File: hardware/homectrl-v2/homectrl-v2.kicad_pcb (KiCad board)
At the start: 2 copper layers, 64 x 64 mm, 136 parts, among them J1 Barrel_Jack, J2 PUMP1_CONN, J3 PUMP2_CONN, J4 STEP_CONN, J5 USB_C_CONN, J6 SMS1_CONN, J7 ALS_CONN, J8 FSW1_CONN, Q1 AO3407A, Q2 2N7002, Q3 ZXMN3A01ZTA, Q4 ZXMN3A01ZTA, Q5 AO3400A, SW1 S3_RESET_SW, SW2 S3_BOOT_SW, U1 TPS5405DR, U2 MCP1826S, U3 DMP4065S-7, U4 ESP32-S3-WROOM-1, U5 TMC2209, U7 TPD4E001DRLR, U8 TPD2E001DRLR, U9 SI2347DS-T1-GE3

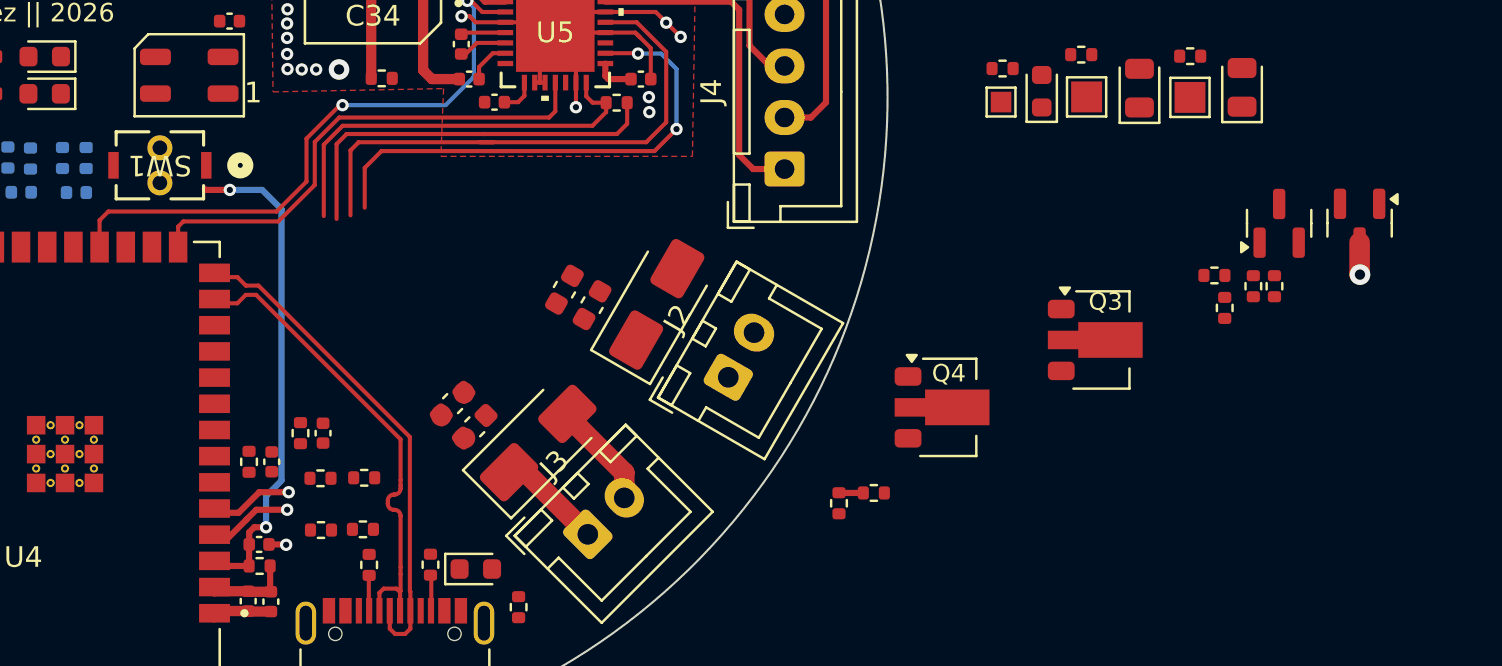
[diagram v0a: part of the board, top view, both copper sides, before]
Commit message: start signal routes
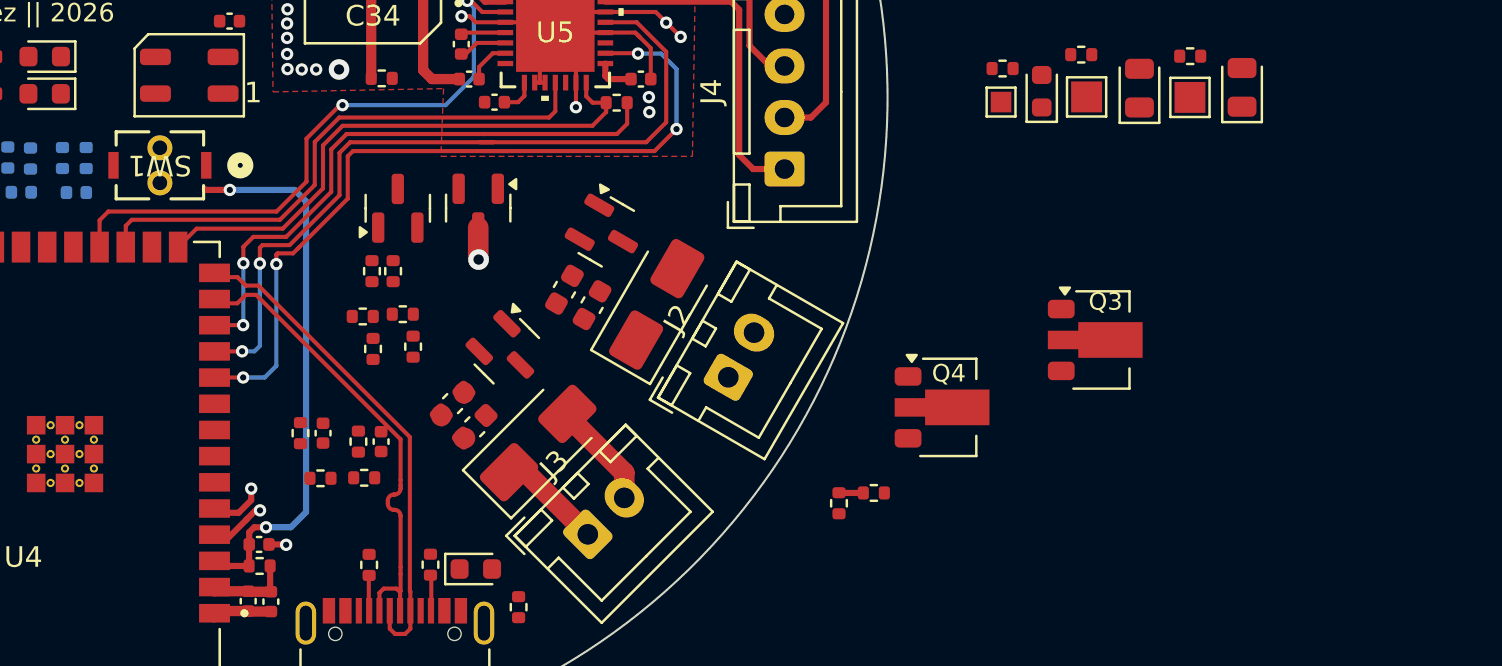
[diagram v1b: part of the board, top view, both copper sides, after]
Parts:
- removed R37: 13k, Resistor_SMD:R_0402_1005Metric
- removed R38: 20K, Resistor_SMD:R_0402_1005Metric
- added R22: 200, Resistor_SMD:R_0402_1005Metric, F.Cu at (134.0, 77.3)
- added R23: 10k, Resistor_SMD:R_0402_1005Metric, F.Cu at (134.5, 78.9)
- added REF**: SOT-23, Package_TO_SOT_SMD:SOT-23, F.Cu at (139.0, 79.1)
- added REF**: SOT-23, Package_TO_SOT_SMD:SOT-23, F.Cu at (143.8, 73.3)
- moved Q2 42.8 mm to (133.7, 72.2)
- moved R6 42.8 mm to (133.5, 75.2)
- moved R7 42.8 mm to (132.5, 75.2)
- moved U3 42.8 mm to (137.6, 72.1)
- moved R22 41.4 mm to (132.0, 77.4)
- moved R23 41.4 mm to (132.5, 79.0)
- moved C28 5.39 mm to (132.9, 83.5)
- moved R39 5.39 mm to (131.8, 83.5)
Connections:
- R22 pad 1: PUMP1_GATE -> PUMP1_EN
- R24 pad 1: PUMP2_GATE -> PUMP2_EN
- U4 pad 10: unconnected-(U4-IO17-Pad10) -> MTR_STEP
- U4 pad 11: unconnected-(U4-IO18-Pad11) -> MTR_DIR
- U4 pad 12: SMS1_DATA -> S3_RXD
- U4 pad 15: STEP_DIAG -> S3_TXD
- U4 pad 17: SMS2_DATA -> STEP_DIAG
- U4 pad 4: VCC_SENSE -> VPLUG_SENSE
- U4 pad 5: VPLUG_SENSE -> SMS1_DATA
- U4 pad 6: unconnected-(U4-IO6-Pad6) -> SMS2_DATA
- U4 pad 7: unconnected-(U4-IO7-Pad7) -> PUMP2_EN
- U4 pad 8: unconnected-(U4-IO15-Pad8) -> PUMP1_EN
- U4 pad 9: unconnected-(U4-IO16-Pad9) -> VPMP_EN
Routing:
- net MTR_STEP: track 25.7 -> 39.7 mm, vias 2 -> 4
- net MTR_DIR: track 26.6 -> 38.1 mm, vias 0 -> 2
- net S3_RXD: track 19.3 -> 28.7 mm, vias 0 -> 2
- net S3_TXD: track 20.0 -> 26.9 mm
- net VCC_SENSE: track 4.13 -> 0.00 mm, vias 1 -> 0
- net SMS1_DATA: track 0.00 -> 2.61 mm, vias 0 -> 1
- net S3_EN: track 24.1 -> 26.7 mm
- net STEP_DIAG: track 24.2 -> 26.8 mm
- net VPLUG_SENSE: track 4.03 -> 2.80 mm

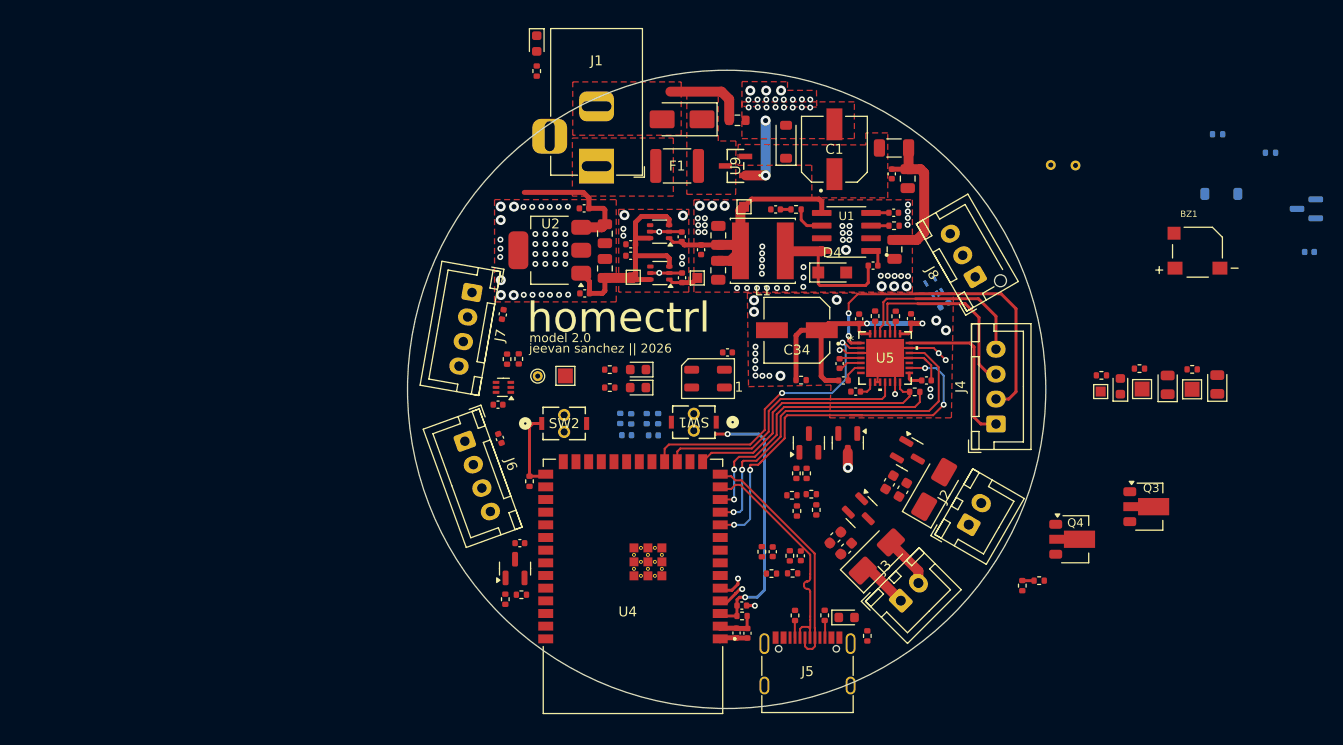
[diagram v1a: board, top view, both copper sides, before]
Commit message: more signal routing
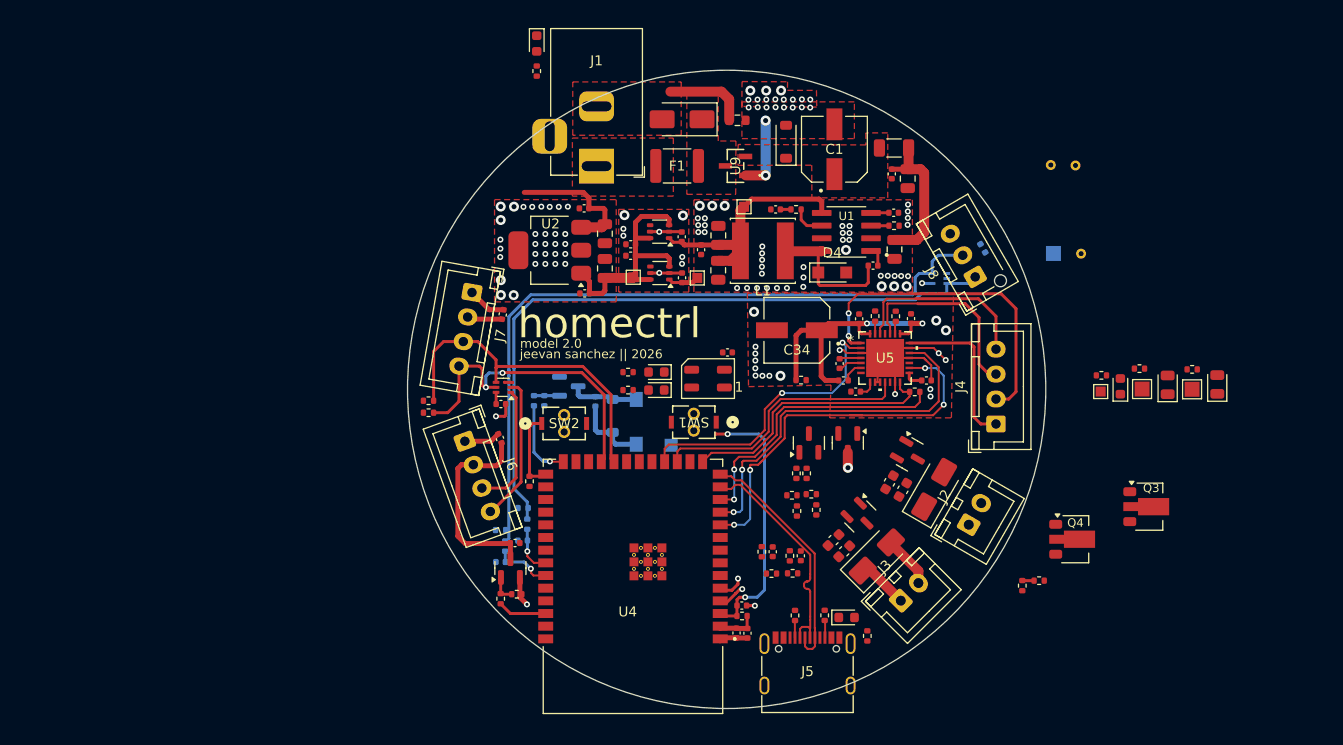
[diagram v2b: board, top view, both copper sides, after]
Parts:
- BZ1, TP1, TP3: moved to B.Cu
- moved R19 76.9 mm to (107.2, 67.9), turned to 90 degrees
- moved Q5 76.1 mm to (109.7, 66.5), turned to 0 degrees
- moved R16 73.6 mm to (106.2, 67.9), turned to -90 degrees
- moved C21 73.2 mm to (112.3, 68.0), turned to 90 degrees
- moved D13 65.0 mm to (114.1, 69.4), turned to 90 degrees
- moved BZ1 57.3 mm to (118.0, 70.0), turned to 90 degrees
- moved TP3 55.9 mm to (161.0, 53.2), turned to 180 degrees
- moved TP1 50.5 mm to (158.3, 53.1), turned to 180 degrees
- moved C24 17.9 mm to (102.8, 84.1), turned to 180 degrees
- moved R32 17.2 mm to (103.3, 82.5)
- moved R28 17.2 mm to (102.8, 80.9), turned to 0 degrees
- moved R27 16.9 mm to (105.5, 80.3)
- moved C32 16.8 mm to (105.0, 81.9), turned to 0 degrees
- moved R26 15.3 mm to (105.1, 78.7), turned to 0 degrees
- moved R34 10.5 mm to (95.6, 69.1), turned to 0 degrees
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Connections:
- C21 pad 2: GND -> Net-(D13-A)
- C24 pad 1: Net-(C24-Pad1) -> FSW2_SIG
- C32 pad 2: Net-(C32-Pad2) -> FSW1_SIG
- J6 pad 3: Net-(J6-Pin_3) -> SMS1_DATA
- J6 pad 4: Net-(J6-Pin_4) -> SMS2_DATA
- R27 pad 1: Net-(C32-Pad2) -> FSW1_SIG
- R32 pad 1: Net-(C24-Pad1) -> FSW2_SIG
- R39 pad 1: Net-(J6-Pin_3) -> SMS1_DATA
- R40 pad 1: Net-(J6-Pin_4) -> SMS2_DATA
- U4 pad 22: unconnected-(U4-IO14-Pad22) -> I2C_CLK
- U4 pad 23: unconnected-(U4-IO21-Pad23) -> I2C_DTA
- U4 pad 26: unconnected-(U4-IO45-Pad26) -> BUZZ_EN
- U4 pad 34: unconnected-(U4-IO41-Pad34) -> FSW1_SIG
- U4 pad 35: unconnected-(U4-IO42-Pad35) -> FSW2_SIG
- U4 pad 38: unconnected-(U4-IO2-Pad38) -> VPMP_EN
- U7 pad 1: SMS2_DATA -> SMS1_DATA
- U7 pad 2: SMS1_DATA -> SMS2_DATA
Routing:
- net FSW2_SIG: track 0.00 -> 78.1 mm, vias 0 -> 1
- net FSW1_SIG: track 0.83 -> 74.9 mm, vias 0 -> 1
- net I2C_CLK: track 0.00 -> 34.2 mm
- net I2C_DTA: track 0.00 -> 33.0 mm, vias 0 -> 2
- net VSMS: track 0.65 -> 21.2 mm
- net +3V3: track 19.3 -> 34.6 mm, vias 0 -> 1
- net SMS2_DATA: track 0.00 -> 14.6 mm
- net SMS1_DATA: track 2.61 -> 15.3 mm
- net GND: track 43.7 -> 55.0 mm, vias 128 -> 122
- net BUZZ_EN: track 0.00 -> 8.00 mm, vias 0 -> 1
- net Net-(D13-A): track 0.00 -> 6.88 mm
- net VPMP_EN: track 0.00 -> 4.92 mm
- net Net-(Q1-G): track 0.00 -> 2.73 mm
- net Net-(Q5-G): track 0.00 -> 2.57 mm

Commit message: finish component routing
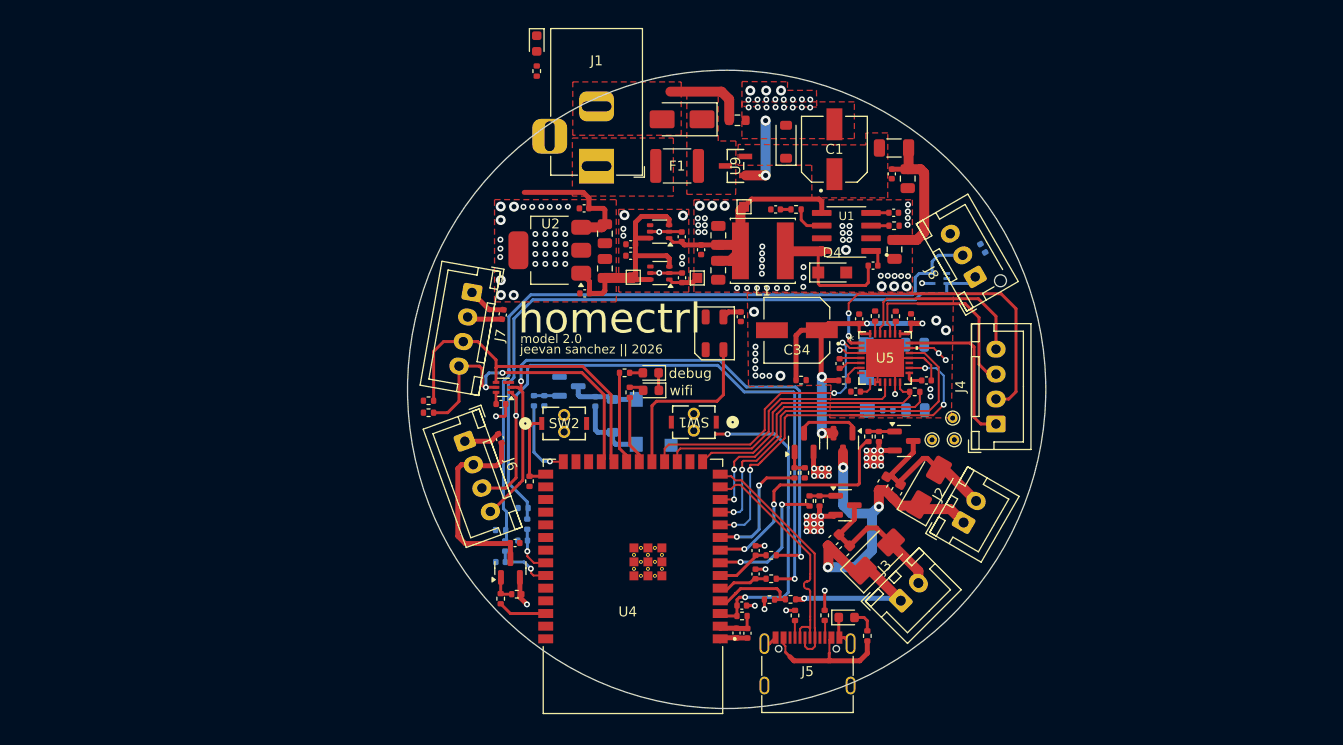
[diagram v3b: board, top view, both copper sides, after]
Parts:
- removed D10: PMP_V_LED, LED_SMD:LED_0603_1608Metric
- removed R15: 1k, Resistor_SMD:R_0402_1005Metric
- removed the R22 at (134.0, 77.3)
- removed the R23 at (134.5, 78.9)
- removed REF** (x2): SOT-23, Package_TO_SOT_SMD:SOT-23
- removed TP2: VMOT_TP_PAD, TestPoint:TestPoint_Pad_1.0x1.0mm
- D7, D8, R12, R13, TP5, TP9: moved to B.Cu
- Q3, Q4: value ZXMN3A01ZTA -> AO3400A; footprint Package_TO_SOT_SMD:SOT-89-3 -> Package_TO_SOT_SMD:SOT-23
- TP13, TP3, TP7: moved to F.Cu
- moved TP9 33.0 mm to (139.5, 62.3), turned to 180 degrees
- moved R13 30.7 mm to (141.6, 62.3)
- moved D8 30.6 mm to (144.4, 62.3), turned to 180 degrees
- moved TP7 30.1 mm to (148.3, 71.8), turned to -90 degrees
- moved TP13 30.0 mm to (146.1, 71.8), turned to -90 degrees
- moved TP5 27.6 mm to (139.6, 68.9), turned to 180 degrees
- moved R12 25.6 mm to (141.7, 68.9)
- moved Q3 25.5 mm to (143.3, 72.0)
- moved D7 25.4 mm to (144.4, 68.9), turned to 180 degrees
- moved R25 23.4 mm to (134.8, 78.0), turned to 90 degrees
- moved Q4 23.3 mm to (137.4, 78.4)
- moved R24 23.0 mm to (133.8, 78.0)
- moved TP1 22.5 mm to (139.5, 65.6)
- moved TP3 20.9 mm to (148.2, 69.7), turned to -90 degrees
- moved R23 11.1 mm to (140.8, 71.5)
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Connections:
- Q3 pad 2: PUMP1_N -> GND
- Q3 pad 3: GND -> PUMP1_N
- Q4 pad 2: PUMP2_N -> GND
- Q4 pad 3: GND -> PUMP2_N
- R8 pad 1: VPLUG -> VPMP
- U4 pad 19: unconnected-(U4-IO11-Pad19) -> RGB_DATA
- U4 pad 20: unconnected-(U4-IO12-Pad20) -> WIFI_LED
- U4 pad 21: unconnected-(U4-IO13-Pad21) -> DBG_LED
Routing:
- net SMS2_DATA: track 14.6 -> 71.4 mm, vias 0 -> 2
- net SMS1_DATA: track 15.3 -> 71.5 mm, vias 1 -> 2
- net GND: track 55.0 -> 106.3 mm, vias 122 -> 151
- net VPMP: track 7.12 -> 52.5 mm, vias 1 -> 4
- net PUMP1_EN: track 0.00 -> 23.2 mm, vias 0 -> 2
- net PUMP1_N: track 0.00 -> 17.8 mm
- net RGB_DATA: track 0.00 -> 17.8 mm
- net 5V_USB: track 3.12 -> 17.2 mm
- net PUMP2_EN: track 0.00 -> 14.0 mm, vias 0 -> 2
- net VPMP_EN: track 4.92 -> 17.4 mm, vias 0 -> 2
- net PUMP2_N: track 5.22 -> 15.8 mm
- net DBG_LED: track 0.00 -> 9.22 mm
- net WIFI_LED: track 0.00 -> 6.84 mm
- net VPLUG: track 44.2 -> 51.0 mm, vias 2 -> 4
- net Net-(Q2-D): track 0.00 -> 6.53 mm
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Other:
- board text added: "debug"
- board text added: "engineered by Jeevan Sanchez in Toronto, CA"
- board text added: "wifi"

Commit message: logic power routing
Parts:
- removed BZ1: SMT-0540-S-R, SMT-0540-S-R:XDCR_SMT-0540-S-R
- removed C21: 0.1uF, Capacitor_SMD:C_0402_1005Metric
- removed D13: 1N4148W, Diode_SMD:D_SOD-123
- removed Q5: AO3400A, Package_TO_SOT_SMD:SOT-23
- removed R16: 200, Resistor_SMD:R_0402_1005Metric
- removed R19: 10k, Resistor_SMD:R_0402_1005Metric
- added D8: 3V3_LED, LED_SMD:LED_0805_2012Metric, F.Cu at (107.8, 66.5)
- added R13: 200, Resistor_SMD:R_0402_1005Metric, F.Cu at (110.6, 66.5)
- D7: value BATT_LED -> PLUG_LED; footprint LED_SMD:LED_0805_2012Metric -> LED_SMD:LED_0603_1608Metric
- J8: footprint Connector_JST:JST_XH_B3B-XH-AM_1x03_P2.50mm_Vertical -> Connector_JST:JST_XH_B3B-XH-A_1x03_P2.50mm_Vertical
- R12: value 1k -> 1K
- TP1: moved to F.Cu
- moved TP13 24.2 mm to (169.2, 64.5)
- moved TP7 24.2 mm to (171.4, 64.5)
- moved TP3 20.2 mm to (128.0, 70.0)
- moved TP1 11.8 mm to (128.0, 67.8), turned to 0 degrees
- moved C31 5.11 mm to (147.0, 55.6), turned to 0 degrees
- moved U8 1.61 mm to (146.6, 57.2)
- moved J4 0.77 mm to (151.7, 70.2)
- moved J5 0.12 mm to (133.6, 95.5)
- turned R39 to 180 degrees
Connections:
- net VPLUG_SENSE renamed VPMP_SENSE
- J6 pad 3: SMS1_DATA -> Net-(J6-Pin_3)
- J6 pad 4: SMS2_DATA -> Net-(J6-Pin_4)
- J8 pad 1: FSW1_SIG -> Net-(J8-Pin_1)
- J8 pad 2: FSW2_SIG -> Net-(J8-Pin_2)
- R26 pad 2: FSW1_SIG -> Net-(J8-Pin_1)
- R27 pad 2: FSW1_SIG -> Net-(J8-Pin_1)
- R28 pad 2: FSW2_SIG -> Net-(J8-Pin_2)
- R32 pad 2: FSW2_SIG -> Net-(J8-Pin_2)
- R39 pad 1: SMS1_DATA -> Net-(J6-Pin_3)
- R40 pad 1: SMS2_DATA -> Net-(J6-Pin_4)
- U7 pad 1: SMS1_DATA -> Net-(J6-Pin_4)
- U7 pad 2: SMS2_DATA -> Net-(J6-Pin_3)
- U8 pad 3: FSW1_SIG -> Net-(J8-Pin_1)
- U8 pad 5: FSW2_SIG -> Net-(J8-Pin_2)
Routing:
- net +3V3: track 36.5 -> 199.6 mm, vias 1 -> 12
- net FSW2_SIG: track 78.4 -> 5.90 mm
- net FSW1_SIG: track 75.3 -> 4.83 mm
- net Net-(J8-Pin_2): track 0.00 -> 69.9 mm
- net Net-(J8-Pin_1): track 0.00 -> 68.8 mm
- net SMS1_DATA: track 71.5 -> 5.09 mm, vias 2 -> 0
- net Net-(J6-Pin_3): track 0.00 -> 66.4 mm, vias 0 -> 2
- net SMS2_DATA: track 71.4 -> 5.51 mm, vias 2 -> 0
- net Net-(J6-Pin_4): track 0.00 -> 65.7 mm, vias 0 -> 2
- net GND: track 106.3 -> 122.4 mm, vias 151 -> 152
- net BUZZ_EN: track 8.00 -> 0.00 mm, vias 1 -> 0
- net Net-(D13-A): track 6.88 -> 0.00 mm
- net VPLUG: track 51.0 -> 57.2 mm
- net Net-(D8-A): track 0.00 -> 2.68 mm
- net Net-(Q5-G): track 2.57 -> 0.00 mm
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
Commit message: board outline done
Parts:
- moved TP13 114.9 mm to (55.4, 48.6)
- moved TP7 114.9 mm to (57.6, 48.6)
- moved U4 0.80 mm to (116.2, 85.7)
- moved J5 0.43 mm to (133.6, 95.9)
- moved D2 0.36 mm to (106.1, 32.1)
- moved J1 0.36 mm to (112.1, 44.4)
- moved R1 0.36 mm to (106.1, 34.8)
- moved J7 0.32 mm to (100.0, 57.4)
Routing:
- net +3V3: track 199.6 -> 198.5 mm
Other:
- board size 64 x 64 mm -> 64 x 70.5 mm
- copper layers 2 -> 4
